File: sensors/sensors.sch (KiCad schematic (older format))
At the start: 0 parts

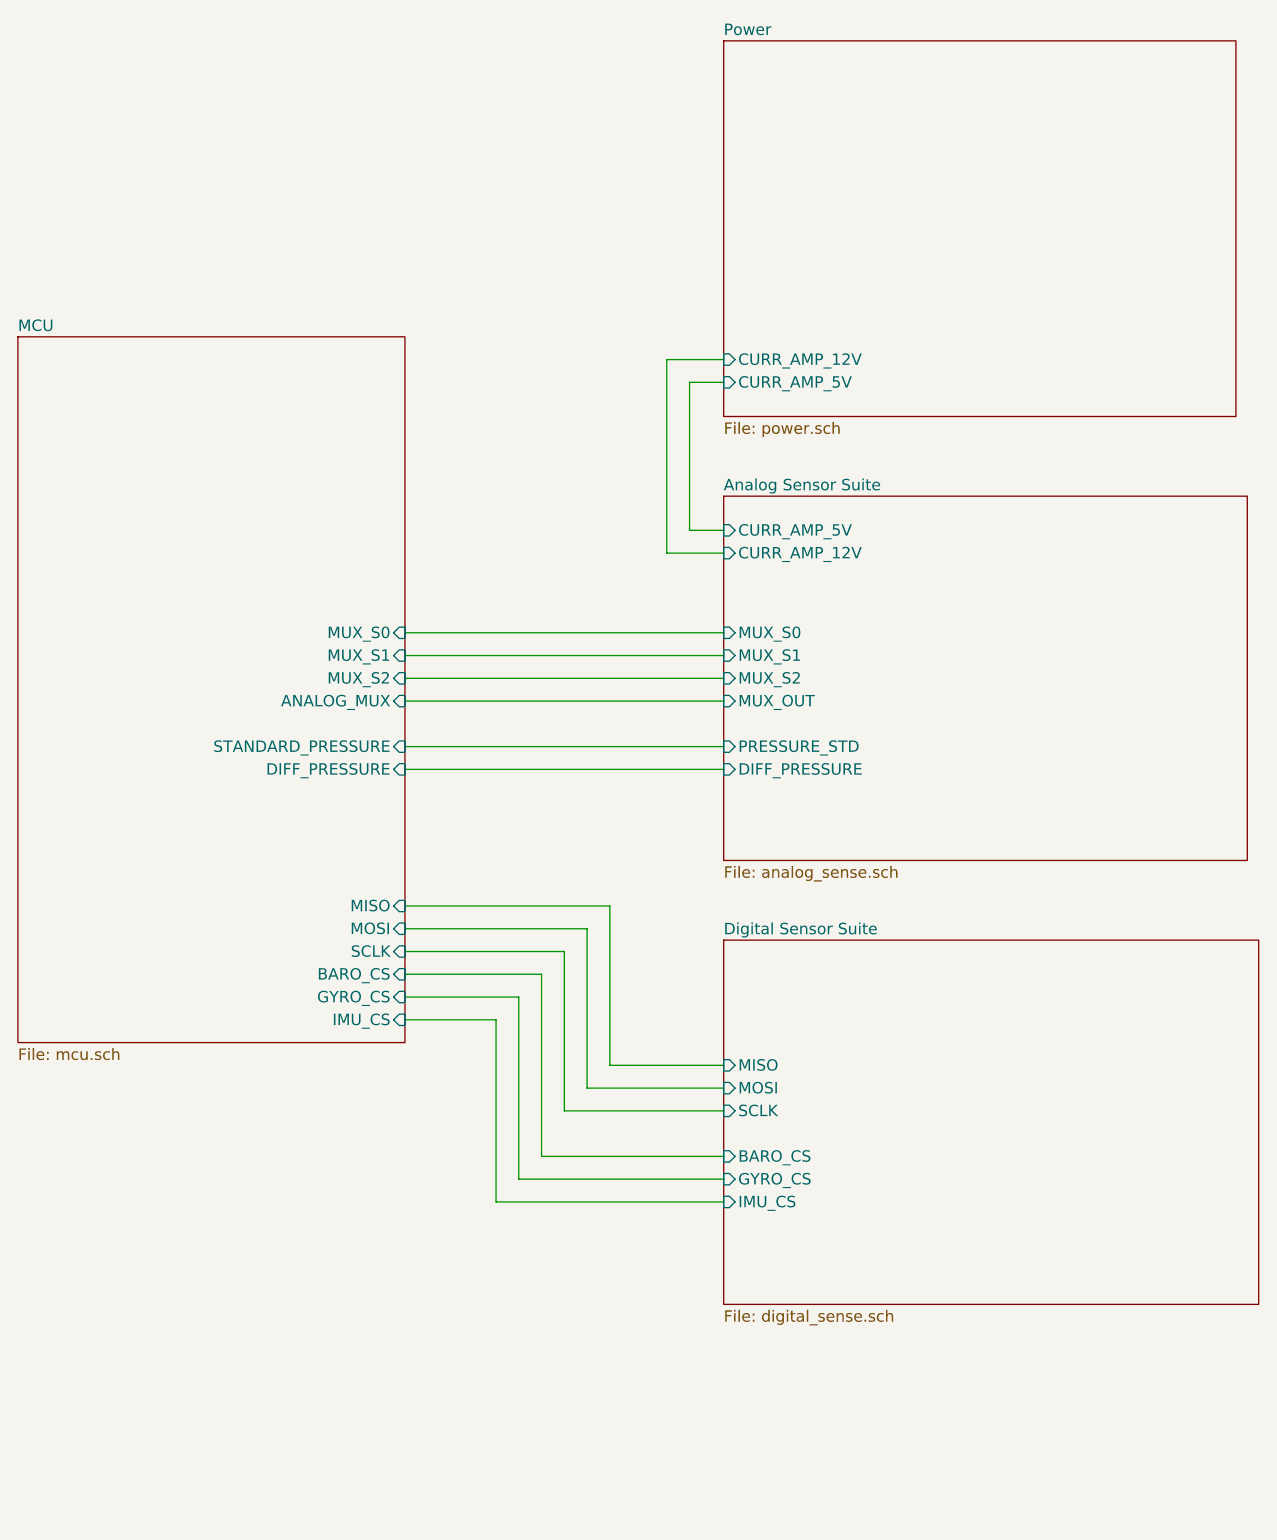
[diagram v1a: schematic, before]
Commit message: Update digital sensor suite
Swap out our old IMUs with a pair of BMX055s. Add all the interfacing
required for that.
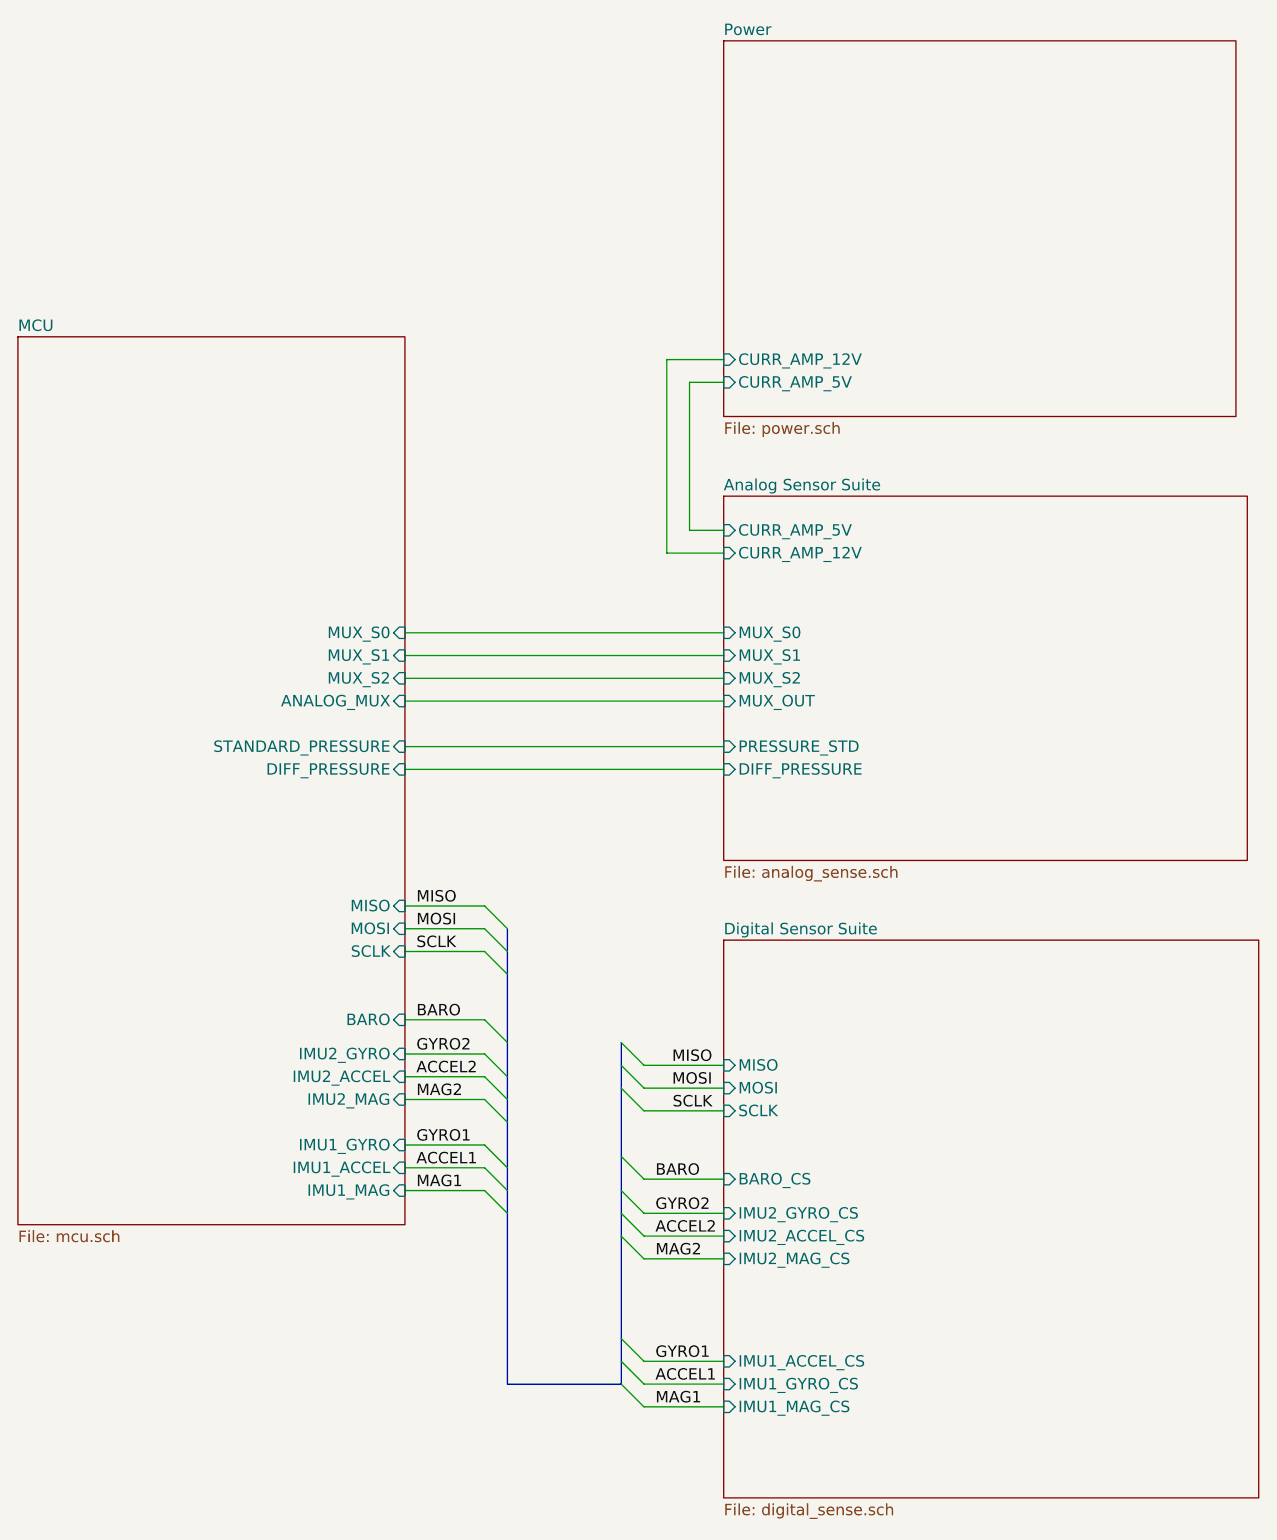
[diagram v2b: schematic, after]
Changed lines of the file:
@@
 EESchema Schematic File Version 4
+LIBS:sensors-cache
 EELAYER 26 0
 EELAYER END
@@
 $EndSheet
 $Sheet
-S 1300 2000 1700 3100
+S 1300 2000 1700 3900
 U 5BB1460E
 F0 "MCU" 50
@@
 F2 "DIFF_PRESSURE" I R 3000 3900 50
 F3 "STANDARD_PRESSURE" I R 3000 3800 50
-F4 "IMU_CS" I R 3000 5000 50
-F5 "GYRO_CS" I R 3000 4900 50
-F6 "BARO_CS" I R 3000 4800 50
-F7 "ANALOG_MUX" I R 3000 3600 50
-F8 "MUX_S0" I R 3000 3300 50
-F9 "MUX_S1" I R 3000 3400 50
-F10 "MUX_S2" I R 3000 3500 50
-F11 "SCLK" I R 3000 4700 50
-F12 "MOSI" I R 3000 4600 50
-F13 "MISO" I R 3000 4500 50
-$EndSheet
-$Sheet
-S 4400 4650 2350 1600
+F4 "ANALOG_MUX" I R 3000 3600 50
+F5 "MUX_S0" I R 3000 3300 50
+F6 "MUX_S1" I R 3000 3400 50
+F7 "MUX_S2" I R 3000 3500 50
+F8 "SCLK" I R 3000 4700 50
+F9 "MOSI" I R 3000 4600 50
+F10 "MISO" I R 3000 4500 50
+F11 "IMU1_ACCEL" I R 3000 5650 50
+F12 "IMU1_GYRO" I R 3000 5550 50
+F13 "IMU1_MAG" I R 3000 5750 50
+F14 "IMU2_ACCEL" I R 3000 5250 50
+F15 "IMU2_GYRO" I R 3000 5150 50
+F16 "IMU2_MAG" I R 3000 5350 50
+F17 "BARO" I R 3000 5000 50
+$EndSheet
+$Sheet
+S 4400 4650 2350 2450
 U 5BB17361
 F0 "Digital Sensor Suite" 50
 F1 "digital_sense.sch" 50
 F2 "MISO" I L 4400 5200 50
-F3 "SCLK" I L 4400 5400 50
-F4 "MOSI" I L 4400 5300 50
-F5 "IMU_CS" I L 4400 5800 50
-F6 "GYRO_CS" I L 4400 5700 50
-F7 "BARO_CS" I L 4400 5600 50
+F3 "MOSI" I L 4400 5300 50
+F4 "BARO_CS" I L 4400 5700 50
+F5 "SCLK" I L 4400 5400 50
+F6 "IMU1_GYRO_CS" I L 4400 6600 50
+F7 "IMU1_ACCEL_CS" I L 4400 6500 50
+F8 "IMU1_MAG_CS" I L 4400 6700 50
+F9 "IMU2_GYRO_CS" I L 4400 5850 50
+F10 "IMU2_ACCEL_CS" I L 4400 5950 50
+F11 "IMU2_MAG_CS" I L 4400 6050 50
 $EndSheet
 $Sheet
@@
 Wire Wire Line
 	3000 3900 4400 3900
-Wire Wire Line
-	3000 5000 3400 5000
-Wire Wire Line
-	3400 5000 3400 5800
-Wire Wire Line
-	3400 5800 4400 5800
-Wire Wire Line
-	3000 4900 3500 4900
-Wire Wire Line
-	3500 4900 3500 5700
-Wire Wire Line
-	3500 5700 4400 5700
-Wire Wire Line
-	3000 4800 3600 4800
-Wire Wire Line
-	3600 4800 3600 5600
-Wire Wire Line
-	3600 5600 4400 5600
-Wire Wire Line
-	3000 4700 3700 4700
-Wire Wire Line
-	3700 4700 3700 5400
-Wire Wire Line
-	3700 5400 4400 5400
-Wire Wire Line
-	3000 4600 3800 4600
-Wire Wire Line
-	3800 5300 4400 5300
-Wire Wire Line
-	3800 4600 3800 5300
-Wire Wire Line
-	3000 4500 3900 4500
-Wire Wire Line
-	3900 4500 3900 5200
-Wire Wire Line
-	3900 5200 4400 5200
+Text Label 3050 4500 0    50   ~ 0
+MISO
+Text Label 3050 4600 0    50   ~ 0
+MOSI
+Text Label 3050 4700 0    50   ~ 0
+SCLK
+Text Label 3050 5000 0    50   ~ 0
+BARO
+Text Label 3050 5150 0    50   ~ 0
+GYRO2
+Text Label 3050 5250 0    50   ~ 0
+ACCEL2
+Text Label 3050 5350 0    50   ~ 0
+MAG2
+Text Label 3050 5550 0    50   ~ 0
+GYRO1
+Text Label 3050 5650 0    50   ~ 0
+ACCEL1
+Text Label 3050 5750 0    50   ~ 0
+MAG1
+Entry Wire Line
+	3350 5650 3450 5750
+Entry Wire Line
+	3350 5750 3450 5850
+Entry Wire Line
+	3350 5550 3450 5650
+Entry Wire Line
+	3350 5350 3450 5450
+Entry Wire Line
+	3350 5250 3450 5350
+Entry Wire Line
+	3350 5150 3450 5250
+Entry Wire Line
+	3350 5000 3450 5100
+Entry Wire Line
+	3350 4700 3450 4800
+Entry Wire Line
+	3350 4600 3450 4700
+Entry Wire Line
+	3350 4500 3450 4600
+Wire Wire Line
+	3000 4500 3350 4500
+Wire Wire Line
+	3000 4600 3350 4600
+Wire Wire Line
+	3000 4700 3350 4700
+Wire Wire Line
+	3000 5000 3350 5000
+Wire Wire Line
+	3000 5150 3350 5150
+Wire Wire Line
+	3000 5250 3350 5250
+Wire Wire Line
+	3000 5350 3350 5350
+Wire Wire Line
+	3000 5550 3350 5550
+Wire Wire Line
+	3000 5650 3350 5650
+Wire Wire Line
+	3000 5750 3350 5750
+Text Label 4350 5200 2    50   ~ 0
+MISO
+Text Label 4350 5300 2    50   ~ 0
+MOSI
+Text Label 4350 5400 2    50   ~ 0
+SCLK
+Wire Wire Line
+	4400 5200 4050 5200
+Wire Wire Line
+	4400 5300 4050 5300
+Wire Wire Line
+	4400 5400 4050 5400
+Text Label 4100 5700 0    50   ~ 0
+BARO
+Text Label 4100 5850 0    50   ~ 0
+GYRO2
+Text Label 4100 5950 0    50   ~ 0
+ACCEL2
+Text Label 4100 6050 0    50   ~ 0
+MAG2
+Wire Wire Line
+	4050 5700 4400 5700
+Wire Wire Line
+	4050 5850 4400 5850
+Wire Wire Line
+	4050 5950 4400 5950
+Wire Wire Line
+	4050 6050 4400 6050
+Text Label 4100 6500 0    50   ~ 0
+GYRO1
+Text Label 4100 6600 0    50   ~ 0
+ACCEL1
+Text Label 4100 6700 0    50   ~ 0
+MAG1
+Wire Wire Line
+	4050 6500 4400 6500
+Wire Wire Line
+	4050 6600 4400 6600
+Wire Wire Line
+	4050 6700 4400 6700
+Entry Wire Line
+	4050 5200 3950 5100
+Entry Wire Line
+	4050 5300 3950 5200
+Entry Wire Line
+	4050 5400 3950 5300
+Entry Wire Line
+	4050 5700 3950 5600
+Entry Wire Line
+	4050 5850 3950 5750
+Entry Wire Line
+	4050 5950 3950 5850
+Entry Wire Line
+	4050 6050 3950 5950
+Entry Wire Line
+	4050 6500 3950 6400
+Entry Wire Line
+	4050 6600 3950 6500
+Entry Wire Line
+	4050 6700 3950 6600
+Wire Bus Line
+	3450 6600 3950 6600
+Wire Bus Line
+	3950 5100 3950 6600
+Wire Bus Line
+	3450 4600 3450 6600
 $EndSCHEMATC

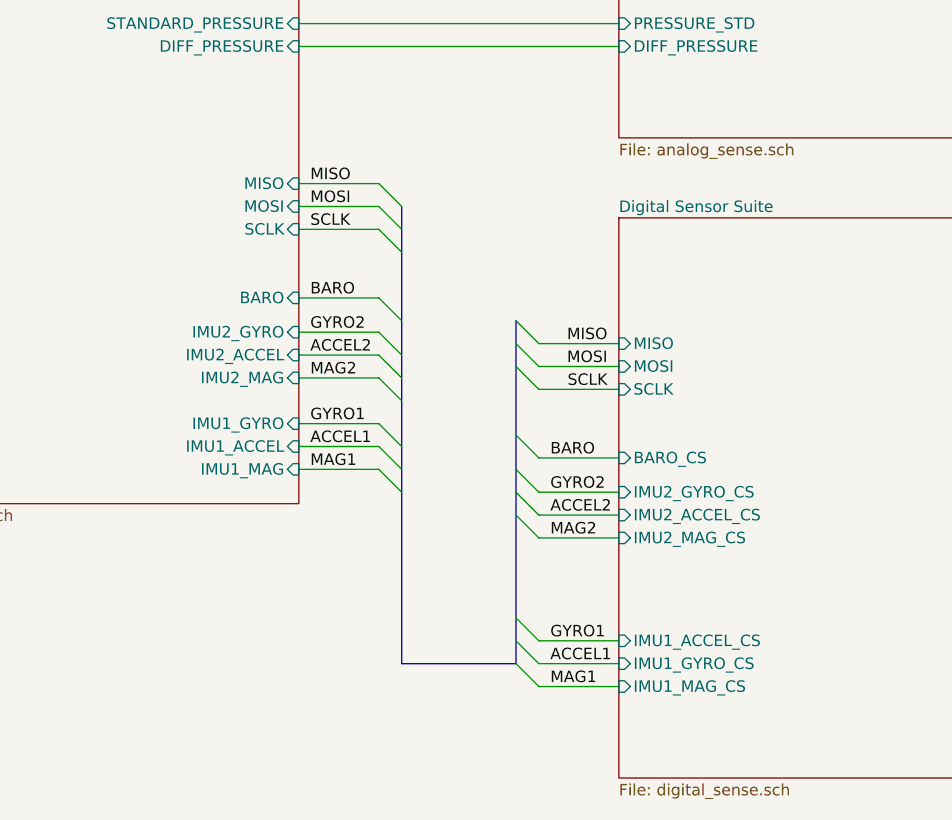
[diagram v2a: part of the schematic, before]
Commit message: Replace IMU cause Jacob wanted to
New IMU has better magnetometer sensitivity
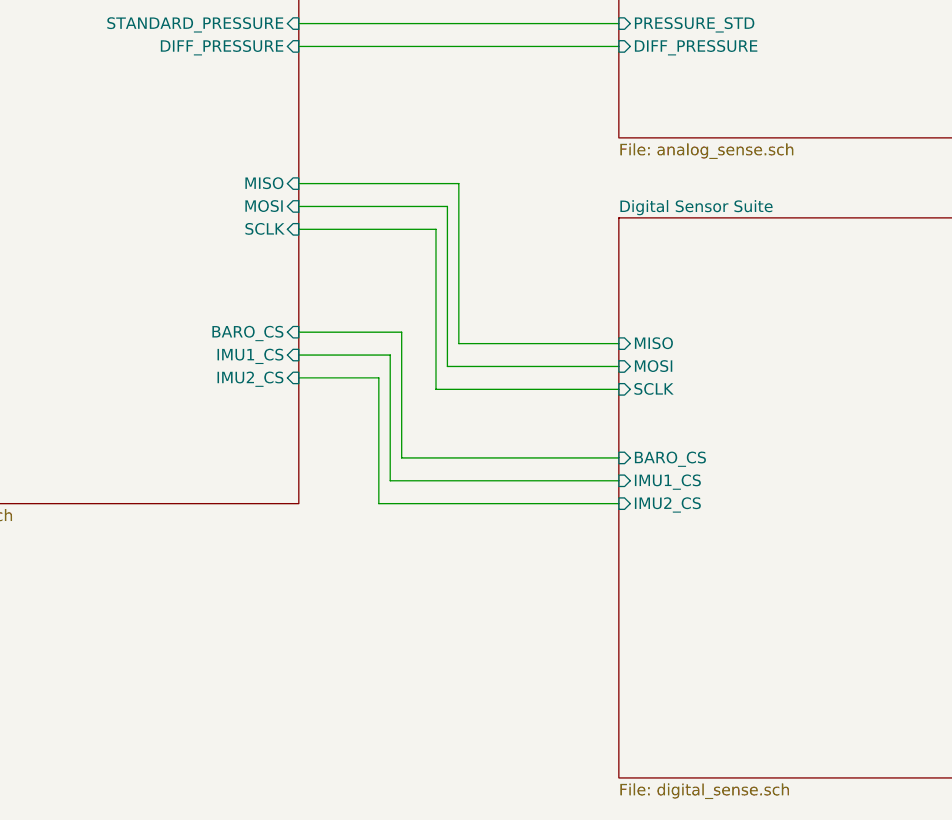
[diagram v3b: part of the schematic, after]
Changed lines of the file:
@@
-$EndSheet
-$Sheet
-S 1300 2000 1700 3900
-U 5BB1460E
-F0 "MCU" 50
-F1 "mcu.sch" 50
-F2 "DIFF_PRESSURE" I R 3000 3900 50
-F3 "STANDARD_PRESSURE" I R 3000 3800 50
-F4 "ANALOG_MUX" I R 3000 3600 50
-F5 "MUX_S0" I R 3000 3300 50
-F6 "MUX_S1" I R 3000 3400 50
-F7 "MUX_S2" I R 3000 3500 50
-F8 "SCLK" I R 3000 4700 50
-F9 "MOSI" I R 3000 4600 50
-F10 "MISO" I R 3000 4500 50
-F11 "IMU1_ACCEL" I R 3000 5650 50
-F12 "IMU1_GYRO" I R 3000 5550 50
-F13 "IMU1_MAG" I R 3000 5750 50
-F14 "IMU2_ACCEL" I R 3000 5250 50
-F15 "IMU2_GYRO" I R 3000 5150 50
-F16 "IMU2_MAG" I R 3000 5350 50
-F17 "BARO" I R 3000 5000 50
 $EndSheet
 $Sheet
@@
 F4 "BARO_CS" I L 4400 5700 50
 F5 "SCLK" I L 4400 5400 50
-F6 "IMU1_GYRO_CS" I L 4400 6600 50
-F7 "IMU1_ACCEL_CS" I L 4400 6500 50
-F8 "IMU1_MAG_CS" I L 4400 6700 50
-F9 "IMU2_GYRO_CS" I L 4400 5850 50
-F10 "IMU2_ACCEL_CS" I L 4400 5950 50
-F11 "IMU2_MAG_CS" I L 4400 6050 50
+F6 "IMU1_CS" I L 4400 5800 50
+F7 "IMU2_CS" I L 4400 5900 50
 $EndSheet
 $Sheet
@@
 Wire Wire Line
 	3000 3900 4400 3900
-Text Label 3050 4500 0    50   ~ 0
-MISO
-Text Label 3050 4600 0    50   ~ 0
-MOSI
-Text Label 3050 4700 0    50   ~ 0
-SCLK
-Text Label 3050 5000 0    50   ~ 0
-BARO
-Text Label 3050 5150 0    50   ~ 0
-GYRO2
-Text Label 3050 5250 0    50   ~ 0
-ACCEL2
-Text Label 3050 5350 0    50   ~ 0
-MAG2
-Text Label 3050 5550 0    50   ~ 0
-GYRO1
-Text Label 3050 5650 0    50   ~ 0
-ACCEL1
-Text Label 3050 5750 0    50   ~ 0
-MAG1
-Entry Wire Line
-	3350 5650 3450 5750
-Entry Wire Line
-	3350 5750 3450 5850
-Entry Wire Line
-	3350 5550 3450 5650
-Entry Wire Line
-	3350 5350 3450 5450
-Entry Wire Line
-	3350 5250 3450 5350
-Entry Wire Line
-	3350 5150 3450 5250
-Entry Wire Line
-	3350 5000 3450 5100
-Entry Wire Line
-	3350 4700 3450 4800
-Entry Wire Line
-	3350 4600 3450 4700
-Entry Wire Line
-	3350 4500 3450 4600
+$Sheet
+S 1300 2000 1700 3900
+U 5BB1460E
+F0 "MCU" 50
+F1 "mcu.sch" 50
+F2 "DIFF_PRESSURE" I R 3000 3900 50
+F3 "STANDARD_PRESSURE" I R 3000 3800 50
+F4 "ANALOG_MUX" I R 3000 3600 50
+F5 "SCLK" I R 3000 4700 50
+F6 "MOSI" I R 3000 4600 50
+F7 "MISO" I R 3000 4500 50
+F8 "BARO_CS" I R 3000 5150 50
+F9 "IMU1_CS" I R 3000 5250 50
+F10 "IMU2_CS" I R 3000 5350 50
+F11 "MUX_S0" I R 3000 3300 50
+F12 "MUX_S1" I R 3000 3400 50
+F13 "MUX_S2" I R 3000 3500 50
+$EndSheet
 Wire Wire Line
-	3000 4500 3350 4500
+	3000 4500 3700 4500
 Wire Wire Line
-	3000 4600 3350 4600
+	3700 4500 3700 5200
 Wire Wire Line
-	3000 4700 3350 4700
+	3700 5200 4400 5200
 Wire Wire Line
-	3000 5000 3350 5000
+	3000 5150 3450 5150
 Wire Wire Line
-	3000 5150 3350 5150
+	3450 5150 3450 5700
 Wire Wire Line
-	3000 5250 3350 5250
+	3450 5700 4400 5700
+Wire Wire Line
+	3000 5250 3400 5250
+Wire Wire Line
+	3400 5250 3400 5800
+Wire Wire Line
+	3400 5800 4400 5800
 Wire Wire Line
 	3000 5350 3350 5350
 Wire Wire Line
-	3000 5550 3350 5550
+	3350 5350 3350 5900
 Wire Wire Line
-	3000 5650 3350 5650
+	3350 5900 4400 5900
 Wire Wire Line
-	3000 5750 3350 5750
-Text Label 4350 5200 2    50   ~ 0
-MISO
-Text Label 4350 5300 2    50   ~ 0
-MOSI
-Text Label 4350 5400 2    50   ~ 0
-SCLK
+	3650 4600 3650 5300
 Wire Wire Line
-	4400 5200 4050 5200
+	3650 5300 4400 5300
 Wire Wire Line
-	4400 5300 4050 5300
+	3000 4600 3650 4600
 Wire Wire Line
-	4400 5400 4050 5400
-Text Label 4100 5700 0    50   ~ 0
-BARO
-Text Label 4100 5850 0    50   ~ 0
-GYRO2
-Text Label 4100 5950 0    50   ~ 0
-ACCEL2
-Text Label 4100 6050 0    50   ~ 0
-MAG2
+	3600 4700 3600 5400
 Wire Wire Line
-	4050 5700 4400 5700
+	3600 5400 4400 5400
 Wire Wire Line
-	4050 5850 4400 5850
-Wire Wire Line
-	4050 5950 4400 5950
-Wire Wire Line
-	4050 6050 4400 6050
-Text Label 4100 6500 0    50   ~ 0
-GYRO1
-Text Label 4100 6600 0    50   ~ 0
-ACCEL1
-Text Label 4100 6700 0    50   ~ 0
-MAG1
-Wire Wire Line
-	4050 6500 4400 6500
-Wire Wire Line
-	4050 6600 4400 6600
-Wire Wire Line
-	4050 6700 4400 6700
-Entry Wire Line
-	4050 5200 3950 5100
-Entry Wire Line
-	4050 5300 3950 5200
-Entry Wire Line
-	4050 5400 3950 5300
-Entry Wire Line
-	4050 5700 3950 5600
-Entry Wire Line
-	4050 5850 3950 5750
-Entry Wire Line
-	4050 5950 3950 5850
-Entry Wire Line
-	4050 6050 3950 5950
-Entry Wire Line
-	4050 6500 3950 6400
-Entry Wire Line
-	4050 6600 3950 6500
-Entry Wire Line
-	4050 6700 3950 6600
-Wire Bus Line
-	3450 6600 3950 6600
-Wire Bus Line
-	3950 5100 3950 6600
-Wire Bus Line
-	3450 4600 3450 6600
+	3000 4700 3600 4700
 $EndSCHEMATC
